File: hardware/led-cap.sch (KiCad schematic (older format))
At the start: 10 parts, among them IC1 ATTINY20-X, K1 CONN_3, P1 CONN_2, P2 CONN_6, Q1 IRLML2402PbF, U1 MMA7660

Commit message: Preliminary layout
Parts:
- removed P2: CONN_6, symbol CONN_6
- added K2: CONN_3, prgm:bcProgramHeader, symbol CONN_3
- added K3: CONN_3, prgm:bcProgramHeader_bottom, symbol CONN_3
- C1, C2: footprint (none) -> Capacitors_SMD:C_0805_HandSoldering
- IC1: footprint TSSOP14 -> tssop-14:TSSOP14
- K1: footprint (none) -> Connect:GS3
- P1: footprint (none) -> mods.pretty:AA Box
- Q1: footprint SOT-23 -> SMD_Packages:SOT-323
- R1, R2: footprint (none) -> Resistors_SMD:R_0603_HandSoldering
- U1: footprint (none) -> mods:DFN-10
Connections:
- net GND: now also K3.3 (P3)
- net VCC: now also K2.2 (PM)
- net LED_DATA: now reaches IC1.10 ((PCINT3/ADC3)PA3), K1.2 (PM)
- net Accel_INT: now reaches IC1.11 ((PCINT2/AIN1/ADC2)PA2), U1.5 (INT)
- net SCL: now reaches IC1.12 ((PCINT1/AIN0/ADC1)PA1), R2.2, U1.6 (SCL)
- net SDA: now reaches IC1.13 ((PCINT0/ADC0)PA0), R1.2, U1.7 (SDA)
- net MOSI: now reaches IC1.3 ((PCINT9/TPIDATA/MOSI/SDA/OC1A)PB1)
- net MOSI: now also K3.1 (P1)
- net RST: now reaches IC1.4 ((PCINT11/~RESET~)PB3)
- net RST: now also K3.2 (PM)
- net MISO: now reaches IC1.5 ((PCINT10/INT0/MISO/OC1B/OC0A/CKOUT)PB2)
- net MISO: now also K2.1 (P1)
- net SCLK: now reaches IC1.6 ((PCINT7/SCL/SCK/T1/ICP1/OC0B/ADC7)PA7)
- net SCLK: now also K2.3 (P3)
- net LED_CTRL: now reaches IC1.9 ((PCINT4/ADC4)PA4), Q1.1 (G)
- net LED_GND: now reaches K1.3 (P3), Q1.3 (D)
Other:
- note removed: "GND\n"
- note removed: "MISO\n"
- note removed: "MOSI"
- note removed: "RST\n"
- note removed: "SCK"
- note removed: "VCC"
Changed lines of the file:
@@
 LIBS:valves
 LIBS:mma7660
+LIBS:led-cap-cache
 EELAYER 24 0
 EELAYER END
@@
 F 0 "IC1" H 2900 4800 40  0000 C CNN
 F 1 "ATTINY20-X" H 4650 3300 40  0000 C CNN
-F 2 "TSSOP14" H 3850 4150 35  0000 C CIN
+F 2 "tssop-14:TSSOP14" H 3850 4150 35  0000 C CIN
 F 3 "" H 3850 4050 60  0000 C CNN
 	1    3850 4050
@@
 F 0 "C1" H 2550 3850 40  0000 L CNN
 F 1 ".1u" H 2556 3665 40  0000 L CNN
-F 2 "" H 2588 3600 30  0000 C CNN
+F 2 "Capacitors_SMD:C_0805_HandSoldering" H 2588 3600 30  0001 C CNN
 F 3 "" H 2550 3750 60  0000 C CNN
 	1    2550 3750
@@
 F 0 "C2" H 8450 4000 40  0000 L CNN
 F 1 "1u" H 8456 3815 40  0000 L CNN
-F 2 "" H 8488 3750 30  0000 C CNN
+F 2 "Capacitors_SMD:C_0805_HandSoldering" H 8488 3750 30  0001 C CNN
 F 3 "" H 8450 3900 60  0000 C CNN
 	1    8450 3900
@@
 F 0 "R1" V 5330 3050 40  0000 C CNN
 F 1 "2k2" V 5257 3051 40  0000 C CNN
-F 2 "" V 5180 3050 30  0000 C CNN
+F 2 "Resistors_SMD:R_0603_HandSoldering" V 5180 3050 30  0001 C CNN
 F 3 "" H 5250 3050 30  0000 C CNN
 	1    5250 3050
@@
 F 0 "R2" V 5580 3050 40  0000 C CNN
 F 1 "2k2" V 5507 3051 40  0000 C CNN
-F 2 "" V 5430 3050 30  0000 C CNN
+F 2 "Resistors_SMD:R_0603_HandSoldering" V 5430 3050 30  0001 C CNN
 F 3 "" H 5500 3050 30  0000 C CNN
 	1    5500 3050
@@
 F 0 "P1" V 3550 2900 40  0000 C CNN
 F 1 "CONN_2" V 3650 2900 40  0000 C CNN
-F 2 "" H 3600 2900 60  0000 C CNN
+F 2 "mods.pretty:AA Box" H 3600 2900 60  0001 C CNN
 F 3 "" H 3600 2900 60  0000 C CNN
 	1    3600 2900
@@
 F 0 "K1" V 8000 3850 50  0000 C CNN
 F 1 "CONN_3" V 8100 3850 40  0000 C CNN
-F 2 "" H 8050 3850 60  0000 C CNN
+F 2 "Connect:GS3" H 8050 3850 60  0001 C CNN
 F 3 "" H 8050 3850 60  0000 C CNN
 	1    8050 3850
-	1    0    0    -1
-$EndComp
-$Comp
-L CONN_6 P2
-U 1 1 54E77A45
-P 6250 4600
-F 0 "P2" V 6200 4600 60  0000 C CNN
-F 1 "CONN_6" V 6300 4600 60  0000 C CNN
-F 2 "" H 6250 4600 60  0000 C CNN
-F 3 "" H 6250 4600 60  0000 C CNN
-	1    6250 4600
 	1    0    0    -1
 $EndComp
@@
 F 0 "U1" H 6350 3000 60  0000 C CNN
 F 1 "MMA7660" H 6500 3650 60  0000 C CNN
-F 2 "" H 6750 3150 60  0000 C CNN
+F 2 "mods:DFN-10" H 6750 3150 60  0001 C CNN
 F 3 "" H 6750 3150 60  0000 C CNN
 	1    6700 3350
@@
 	2550 3450 2700 3450
 Wire Wire Line
-	2550 3300 2550 3450
-Wire Wire Line
-	2550 3450 2550 3550
+	2550 3300 2550 3550
 $Comp
 L GND #PWR2
@@
 	5550 4150 5000 4150
 Wire Wire Line
-	5900 4650 5450 4650
-Wire Wire Line
-	5450 4650 5450 4450
+	5900 4700 5450 4700
+Wire Wire Line
+	5450 4700 5450 4450
 Wire Wire Line
 	5450 4450 5000 4450
 Wire Wire Line
-	5900 4750 5200 4750
-Wire Wire Line
-	5200 4750 5200 4650
+	5900 4800 5200 4800
+Wire Wire Line
+	5200 4800 5200 4650
 Wire Wire Line
 	5200 4650 5000 4650
 Wire Wire Line
-	5900 4850 5800 4850
-Wire Wire Line
-	5800 4850 5800 4950
+	5900 4900 5750 4900
+Wire Wire Line
+	5750 4900 5750 5000
 $Comp
 L VCC #PWR8
@@
 $EndComp
 $Comp
-L GND #PWR10
+L GND #PWR9
 U 1 1 54E77FCD
-P 5800 4950
-F 0 "#PWR10" H 5800 4950 30  0001 C CNN
-F 1 "GND" H 5800 4880 30  0001 C CNN
-F 2 "" H 5800 4950 60  0000 C CNN
-F 3 "" H 5800 4950 60  0000 C CNN
-	1    5800 4950
-	1    0    0    -1
-$EndComp
-Text Notes 5750 4350 0    60   ~ 0
-MISO\n
-Text Notes 5750 4450 0    60   ~ 0
-VCC
-Text Notes 5750 4550 0    60   ~ 0
-SCK
-Text Notes 5750 4650 0    60   ~ 0
-MOSI
-Text Notes 5750 4750 0    60   ~ 0
-RST\n
-Text Notes 5750 4850 0    60   ~ 0
-GND\n
-Wire Wire Line
-	5000 3450 5250 3450
-Wire Wire Line
-	5250 3450 5950 3450
-Wire Wire Line
-	5000 3550 5500 3550
-Wire Wire Line
-	5500 3550 5950 3550
+P 5750 5000
+F 0 "#PWR9" H 5750 5000 30  0001 C CNN
+F 1 "GND" H 5750 4930 30  0001 C CNN
+F 2 "" H 5750 5000 60  0000 C CNN
+F 3 "" H 5750 5000 60  0000 C CNN
+	1    5750 5000
+	1    0    0    -1
+$EndComp
+Wire Wire Line
+	5000 3450 5950 3450
+Wire Wire Line
+	5000 3550 5950 3550
 Wire Wire Line
 	7400 3550 7400 3750
@@
 	7700 4600 7700 4500
 Wire Wire Line
-	7700 3500 7700 3600
-Wire Wire Line
-	7700 3600 7700 3750
+	7700 3500 7700 3750
 Wire Wire Line
 	5250 3300 5250 3450
@@
 $EndComp
 $Comp
-L VCC #PWR9
+L VCC #PWR10
 U 1 1 54E7825F
 P 5800 2800
-F 0 "#PWR9" H 5800 2900 30  0001 C CNN
+F 0 "#PWR10" H 5800 2900 30  0001 C CNN
 F 1 "VCC" H 5800 2900 30  0000 C CNN
 F 2 "" H 5800 2800 60  0000 C CNN
@@
 F 0 "Q1" H 7600 4151 40  0000 R CNN
 F 1 "IRLML2402PbF" H 8250 4350 40  0000 R CNN
-F 2 "SOT-23" H 7470 4402 29  0000 C CNN
+F 2 "SMD_Packages:SOT-323" H 7470 4402 29  0000 C CNN
 F 3 "" H 7600 4300 60  0000 C CNN
 	1    7600 4300
 	1    0    0    -1
 $EndComp
+$Comp
+L CONN_3 K2
+U 1 1 54EDFF11
+P 6250 4450
+F 0 "K2" V 6200 4450 50  0000 C CNN
+F 1 "CONN_3" V 6300 4450 40  0000 C CNN
+F 2 "prgm:bcProgramHeader" H 6250 4450 60  0001 C CNN
+F 3 "" H 6250 4450 60  0000 C CNN
+	1    6250 4450
+	1    0    0    -1
+$EndComp
+$Comp
+L CONN_3 K3
+U 1 1 54EDFFA4
+P 6250 4800
+F 0 "K3" V 6200 4800 50  0000 C CNN
+F 1 "CONN_3" V 6300 4800 40  0000 C CNN
+F 2 "prgm:bcProgramHeader_bottom" H 6250 4800 60  0001 C CNN
+F 3 "" H 6250 4800 60  0000 C CNN
+	1    6250 4800
+	1    0    0    -1
+$EndComp
+Text Label 5600 3450 0    60   ~ 0
+SDA
+Text Label 5600 3550 0    60   ~ 0
+SCL
+Text Label 5750 4350 0    60   ~ 0
+MISO
+Text Label 5750 4700 0    60   ~ 0
+MOSI
+Text Label 5750 4800 0    60   ~ 0
+RST
+Text Label 5750 4900 0    60   ~ 0
+GND
+Text Label 5750 4450 0    60   ~ 0
+VCC
+Text Label 5750 4550 0    60   ~ 0
+SCLK
+Text Label 5100 3750 0    60   ~ 0
+LED_DATA
+Text Label 5100 3850 0    60   ~ 0
+LED_CTRL
+Text Label 6450 3750 0    60   ~ 0
+Accel_INT
+Text Label 7700 4100 0    60   ~ 0
+LED_GND
 $EndSCHEMATC

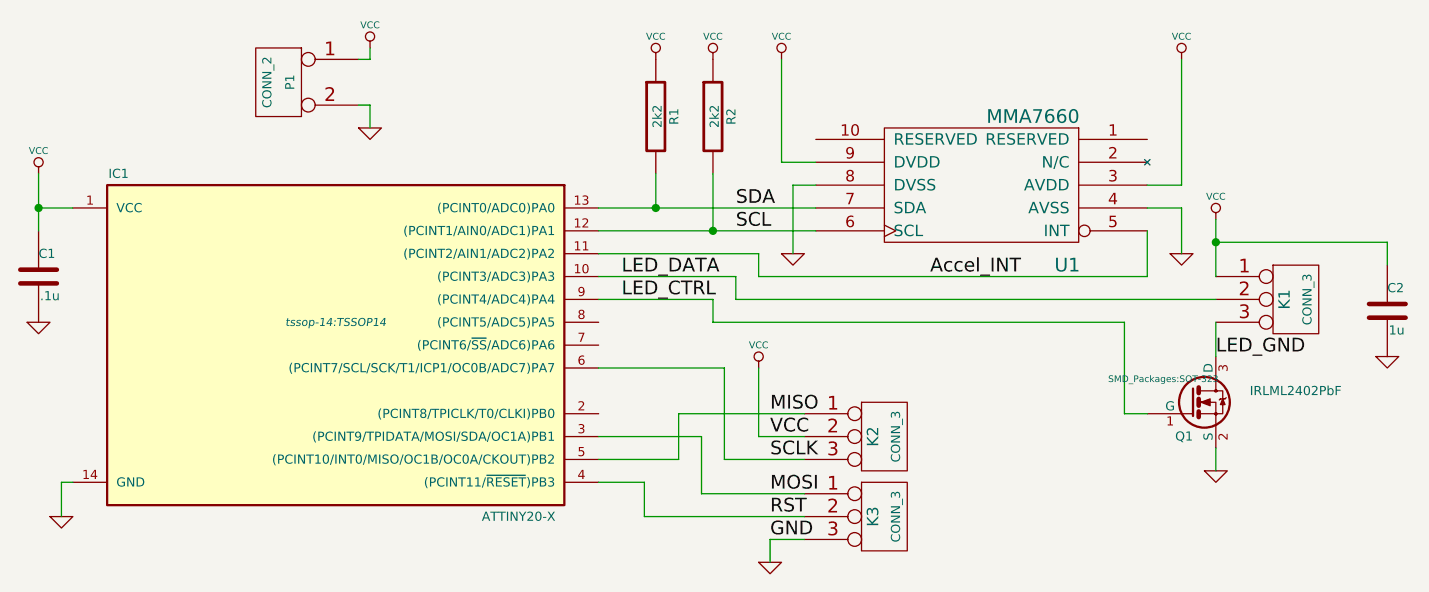
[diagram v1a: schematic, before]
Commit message: Updating based on Sheaff & Segee recommendations
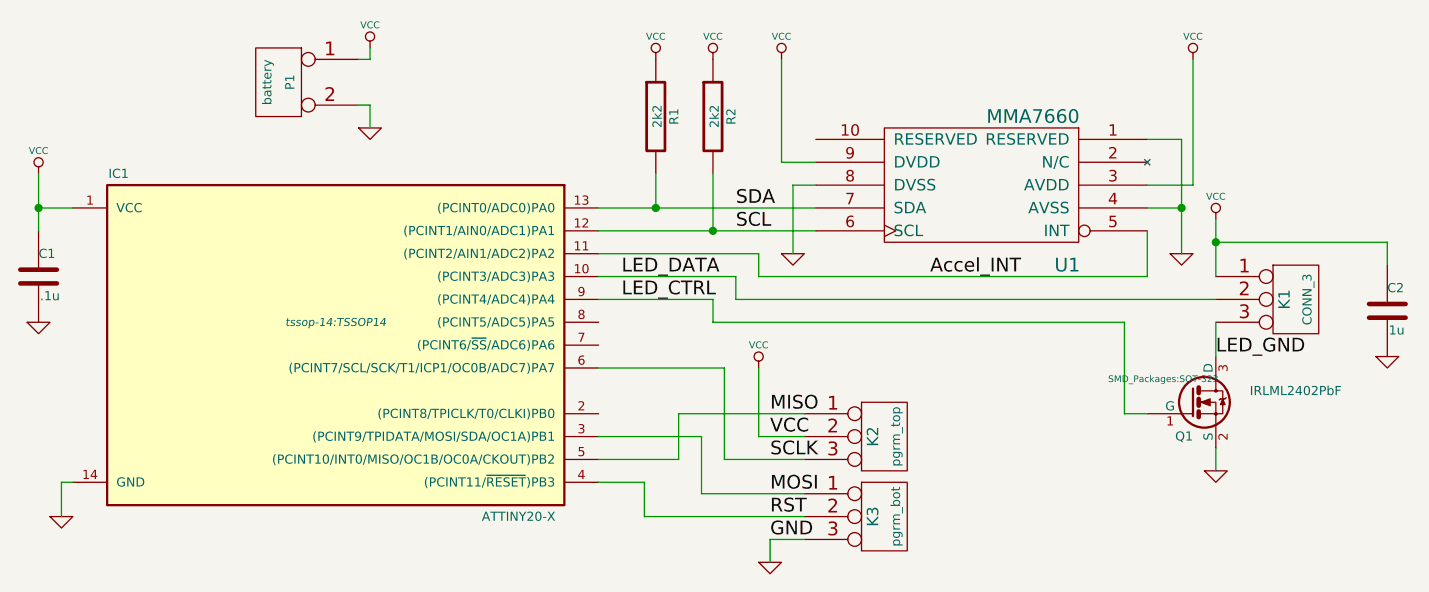
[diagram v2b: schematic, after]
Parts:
- K2: value CONN_3 -> pgrm_top
- K3: value CONN_3 -> pgrm_bot
- P1: value CONN_2 -> battery
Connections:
- net GND: now also U1.1 (RESERVED)
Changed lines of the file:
@@
 P 3600 2900
 F 0 "P1" V 3550 2900 40  0000 C CNN
-F 1 "CONN_2" V 3650 2900 40  0000 C CNN
+F 1 "battery" V 3650 2900 40  0000 C CNN
 F 2 "mods.pretty:AA Box" H 3600 2900 60  0001 C CNN
 F 3 "" H 3600 2900 60  0000 C CNN
@@
 $EndComp
 $Comp
-L GND #PWR3
+L GND #PWR01
 U 1 1 54E77E6C
 P 2650 4800
-F 0 "#PWR3" H 2650 4800 30  0001 C CNN
+F 0 "#PWR01" H 2650 4800 30  0001 C CNN
 F 1 "GND" H 2650 4730 30  0001 C CNN
 F 2 "" H 2650 4800 60  0000 C CNN
@@
 	1    0    0    -1
 $EndComp
-Wire Wire Line
-	2700 4650 2650 4650
-Wire Wire Line
-	2650 4650 2650 4800
-$Comp
-L VCC #PWR1
+$Comp
+L VCC #PWR02
 U 1 1 54E77E87
 P 2550 3300
-F 0 "#PWR1" H 2550 3400 30  0001 C CNN
+F 0 "#PWR02" H 2550 3400 30  0001 C CNN
 F 1 "VCC" H 2550 3400 30  0000 C CNN
 F 2 "" H 2550 3300 60  0000 C CNN
@@
 	1    0    0    -1
 $EndComp
-Wire Wire Line
-	2550 3450 2700 3450
-Wire Wire Line
-	2550 3300 2550 3550
-$Comp
-L GND #PWR2
+$Comp
+L GND #PWR03
 U 1 1 54E77E9E
 P 2550 3950
-F 0 "#PWR2" H 2550 3950 30  0001 C CNN
+F 0 "#PWR03" H 2550 3950 30  0001 C CNN
 F 1 "GND" H 2550 3880 30  0001 C CNN
 F 2 "" H 2550 3950 60  0000 C CNN
@@
 $EndComp
 $Comp
-L GND #PWR5
+L GND #PWR04
 U 1 1 54E77EB1
 P 4000 3100
-F 0 "#PWR5" H 4000 3100 30  0001 C CNN
+F 0 "#PWR04" H 4000 3100 30  0001 C CNN
 F 1 "GND" H 4000 3030 30  0001 C CNN
 F 2 "" H 4000 3100 60  0000 C CNN
@@
 $EndComp
 $Comp
-L VCC #PWR4
+L VCC #PWR05
 U 1 1 54E77EBE
 P 4000 2750
-F 0 "#PWR4" H 4000 2850 30  0001 C CNN
+F 0 "#PWR05" H 4000 2850 30  0001 C CNN
 F 1 "VCC" H 4000 2850 30  0000 C CNN
 F 2 "" H 4000 2750 60  0000 C CNN
@@
 	1    0    0    -1
 $EndComp
-Wire Wire Line
-	3950 2800 4000 2800
-Wire Wire Line
-	4000 2800 4000 2750
-Wire Wire Line
-	3950 3000 4000 3000
-Wire Wire Line
-	4000 3000 4000 3100
-Wire Wire Line
-	5000 4550 5350 4550
-Wire Wire Line
-	5350 4550 5350 4350
-Wire Wire Line
-	5350 4350 5900 4350
-Wire Wire Line
-	5900 4450 5700 4450
-Wire Wire Line
-	5700 4450 5700 4150
-Wire Wire Line
-	5900 4550 5550 4550
-Wire Wire Line
-	5550 4550 5550 4150
-Wire Wire Line
-	5550 4150 5000 4150
-Wire Wire Line
-	5900 4700 5450 4700
-Wire Wire Line
-	5450 4700 5450 4450
-Wire Wire Line
-	5450 4450 5000 4450
-Wire Wire Line
-	5900 4800 5200 4800
-Wire Wire Line
-	5200 4800 5200 4650
-Wire Wire Line
-	5200 4650 5000 4650
-Wire Wire Line
-	5900 4900 5750 4900
-Wire Wire Line
-	5750 4900 5750 5000
-$Comp
-L VCC #PWR8
+$Comp
+L VCC #PWR06
 U 1 1 54E77FB7
 P 5700 4150
-F 0 "#PWR8" H 5700 4250 30  0001 C CNN
+F 0 "#PWR06" H 5700 4250 30  0001 C CNN
 F 1 "VCC" H 5700 4250 30  0000 C CNN
 F 2 "" H 5700 4150 60  0000 C CNN
@@
 $EndComp
 $Comp
-L GND #PWR9
+L GND #PWR07
 U 1 1 54E77FCD
 P 5750 5000
-F 0 "#PWR9" H 5750 5000 30  0001 C CNN
+F 0 "#PWR07" H 5750 5000 30  0001 C CNN
 F 1 "GND" H 5750 4930 30  0001 C CNN
 F 2 "" H 5750 5000 60  0000 C CNN
@@
 	1    0    0    -1
 $EndComp
-Wire Wire Line
-	5000 3450 5950 3450
-Wire Wire Line
-	5000 3550 5950 3550
-Wire Wire Line
-	7400 3550 7400 3750
-Wire Wire Line
-	7400 3750 5700 3750
-Wire Wire Line
-	5700 3750 5700 3650
-Wire Wire Line
-	5700 3650 5000 3650
-Wire Wire Line
-	5000 3750 5600 3750
-Wire Wire Line
-	5600 3750 5600 3850
-Wire Wire Line
-	5600 3850 7700 3850
-Wire Wire Line
-	7700 3950 7700 4100
-Wire Wire Line
-	5000 3850 5500 3850
-Wire Wire Line
-	5500 3850 5500 3950
-Wire Wire Line
-	5500 3950 7300 3950
-Wire Wire Line
-	7300 3950 7300 4350
-Wire Wire Line
-	7300 4350 7400 4350
-$Comp
-L VCC #PWR14
+$Comp
+L VCC #PWR08
 U 1 1 54E78138
 P 7700 3500
-F 0 "#PWR14" H 7700 3600 30  0001 C CNN
+F 0 "#PWR08" H 7700 3600 30  0001 C CNN
 F 1 "VCC" H 7700 3600 30  0000 C CNN
 F 2 "" H 7700 3500 60  0000 C CNN
@@
 $EndComp
 $Comp
-L GND #PWR15
+L GND #PWR09
 U 1 1 54E78143
 P 7700 4600
-F 0 "#PWR15" H 7700 4600 30  0001 C CNN
+F 0 "#PWR09" H 7700 4600 30  0001 C CNN
 F 1 "GND" H 7700 4530 30  0001 C CNN
 F 2 "" H 7700 4600 60  0000 C CNN
@@
 	1    0    0    -1
 $EndComp
-Wire Wire Line
-	7700 4600 7700 4500
-Wire Wire Line
-	7700 3500 7700 3750
-Wire Wire Line
-	5250 3300 5250 3450
-Connection ~ 5250 3450
-Wire Wire Line
-	5500 3300 5500 3550
-Connection ~ 5500 3550
-$Comp
-L VCC #PWR6
+$Comp
+L VCC #PWR010
 U 1 1 54E78219
 P 5250 2800
-F 0 "#PWR6" H 5250 2900 30  0001 C CNN
+F 0 "#PWR010" H 5250 2900 30  0001 C CNN
 F 1 "VCC" H 5250 2900 30  0000 C CNN
 F 2 "" H 5250 2800 60  0000 C CNN
@@
 $EndComp
 $Comp
-L VCC #PWR7
+L VCC #PWR011
 U 1 1 54E78224
 P 5500 2800
-F 0 "#PWR7" H 5500 2900 30  0001 C CNN
+F 0 "#PWR011" H 5500 2900 30  0001 C CNN
 F 1 "VCC" H 5500 2900 30  0000 C CNN
 F 2 "" H 5500 2800 60  0000 C CNN
@@
 $EndComp
 $Comp
-L VCC #PWR10
+L VCC #PWR012
 U 1 1 54E7825F
 P 5800 2800
-F 0 "#PWR10" H 5800 2900 30  0001 C CNN
+F 0 "#PWR012" H 5800 2900 30  0001 C CNN
 F 1 "VCC" H 5800 2900 30  0000 C CNN
 F 2 "" H 5800 2800 60  0000 C CNN
@@
 $EndComp
 $Comp
-L VCC #PWR12
+L VCC #PWR013
 U 1 1 54E7826A
-P 7550 2800
-F 0 "#PWR12" H 7550 2900 30  0001 C CNN
-F 1 "VCC" H 7550 2900 30  0000 C CNN
-F 2 "" H 7550 2800 60  0000 C CNN
-F 3 "" H 7550 2800 60  0000 C CNN
-	1    7550 2800
-	1    0    0    -1
-$EndComp
-Wire Wire Line
-	7400 3350 7550 3350
-Wire Wire Line
-	5950 3250 5800 3250
-Wire Wire Line
-	5800 3250 5800 2800
-$Comp
-L GND #PWR13
+P 7600 2800
+F 0 "#PWR013" H 7600 2900 30  0001 C CNN
+F 1 "VCC" H 7600 2900 30  0000 C CNN
+F 2 "" H 7600 2800 60  0000 C CNN
+F 3 "" H 7600 2800 60  0000 C CNN
+	1    7600 2800
+	1    0    0    -1
+$EndComp
+$Comp
+L GND #PWR014
 U 1 1 54E7830A
 P 7550 3650
-F 0 "#PWR13" H 7550 3650 30  0001 C CNN
+F 0 "#PWR014" H 7550 3650 30  0001 C CNN
 F 1 "GND" H 7550 3580 30  0001 C CNN
 F 2 "" H 7550 3650 60  0000 C CNN
@@
 $EndComp
 $Comp
-L GND #PWR11
+L GND #PWR015
 U 1 1 54E78315
 P 5850 3650
-F 0 "#PWR11" H 5850 3650 30  0001 C CNN
+F 0 "#PWR015" H 5850 3650 30  0001 C CNN
 F 1 "GND" H 5850 3580 30  0001 C CNN
 F 2 "" H 5850 3650 60  0000 C CNN
@@
 	1    0    0    -1
 $EndComp
-Wire Wire Line
-	5950 3350 5850 3350
-Wire Wire Line
-	5850 3350 5850 3650
-Wire Wire Line
-	7400 3450 7550 3450
-Wire Wire Line
-	7550 3450 7550 3650
-$Comp
-L GND #PWR16
+$Comp
+L GND #PWR016
 U 1 1 54E78405
 P 8450 4100
-F 0 "#PWR16" H 8450 4100 30  0001 C CNN
+F 0 "#PWR016" H 8450 4100 30  0001 C CNN
 F 1 "GND" H 8450 4030 30  0001 C CNN
 F 2 "" H 8450 4100 60  0000 C CNN
@@
 	1    0    0    -1
 $EndComp
-Wire Wire Line
-	7700 3600 8450 3600
-Wire Wire Line
-	8450 3600 8450 3700
-Connection ~ 7700 3600
-Wire Wire Line
-	7550 3350 7550 2800
-Connection ~ 2550 3450
 $Comp
 L BSS138 Q1
@@
 P 6250 4450
 F 0 "K2" V 6200 4450 50  0000 C CNN
-F 1 "CONN_3" V 6300 4450 40  0000 C CNN
+F 1 "pgrm_top" V 6300 4450 40  0000 C CNN
 F 2 "prgm:bcProgramHeader" H 6250 4450 60  0001 C CNN
 F 3 "" H 6250 4450 60  0000 C CNN
@@
 P 6250 4800
 F 0 "K3" V 6200 4800 50  0000 C CNN
-F 1 "CONN_3" V 6300 4800 40  0000 C CNN
+F 1 "pgrm_bot" V 6300 4800 40  0000 C CNN
 F 2 "prgm:bcProgramHeader_bottom" H 6250 4800 60  0001 C CNN
 F 3 "" H 6250 4800 60  0000 C CNN
@@
 Text Label 7700 4100 0    60   ~ 0
 LED_GND
+Wire Wire Line
+	2700 4650 2650 4650
+Wire Wire Line
+	2650 4650 2650 4800
+Wire Wire Line
+	2550 3450 2700 3450
+Wire Wire Line
+	2550 3300 2550 3550
+Wire Wire Line
+	3950 2800 4000 2800
+Wire Wire Line
+	4000 2800 4000 2750
+Wire Wire Line
+	3950 3000 4000 3000
+Wire Wire Line
+	4000 3000 4000 3100
+Wire Wire Line
+	5000 4550 5350 4550
+Wire Wire Line
+	5350 4550 5350 4350
+Wire Wire Line
+	5350 4350 5900 4350
+Wire Wire Line
+	5900 4450 5700 4450
+Wire Wire Line
+	5700 4450 5700 4150
+Wire Wire Line
+	5900 4550 5550 4550
+Wire Wire Line
+	5550 4550 5550 4150
+Wire Wire Line
+	5550 4150 5000 4150
+Wire Wire Line
+	5900 4700 5450 4700
+Wire Wire Line
+	5450 4700 5450 4450
+Wire Wire Line
+	5450 4450 5000 4450
+Wire Wire Line
+	5900 4800 5200 4800
+Wire Wire Line
+	5200 4800 5200 4650
+Wire Wire Line
+	5200 4650 5000 4650
+Wire Wire Line
+	5900 4900 5750 4900
+Wire Wire Line
+	5750 4900 5750 5000
+Wire Wire Line
+	5000 3450 5950 3450
+Wire Wire Line
+	5000 3550 5950 3550
+Wire Wire Line
+	7400 3550 7400 3750
+Wire Wire Line
+	7400 3750 5700 3750
+Wire Wire Line
+	5700 3750 5700 3650
+Wire Wire Line
+	5700 3650 5000 3650
+Wire Wire Line
+	5000 3750 5600 3750
+Wire Wire Line
+	5600 3750 5600 3850
+Wire Wire Line
+	5600 3850 7700 3850
+Wire Wire Line
+	7700 3950 7700 4100
+Wire Wire Line
+	5000 3850 5500 3850
+Wire Wire Line
+	5500 3850 5500 3950
+Wire Wire Line
+	5500 3950 7300 3950
+Wire Wire Line
+	7300 3950 7300 4350
+Wire Wire Line
+	7300 4350 7400 4350
+Wire Wire Line
+	7700 4600 7700 4500
+Wire Wire Line
+	7700 3500 7700 3750
+Wire Wire Line
+	5250 3300 5250 3450
+Connection ~ 5250 3450
+Wire Wire Line
+	5500 3300 5500 3550
+Connection ~ 5500 3550
+Wire Wire Line
+	7400 3350 7600 3350
+Wire Wire Line
+	5950 3250 5800 3250
+Wire Wire Line
+	5800 3250 5800 2800
+Wire Wire Line
+	5950 3350 5850 3350
+Wire Wire Line
+	5850 3350 5850 3650
+Wire Wire Line
+	7400 3450 7550 3450
+Wire Wire Line
+	7550 3150 7550 3650
+Wire Wire Line
+	7700 3600 8450 3600
+Wire Wire Line
+	8450 3600 8450 3700
+Connection ~ 7700 3600
+Wire Wire Line
+	7600 3350 7600 2800
+Connection ~ 2550 3450
+Wire Wire Line
+	7400 3150 7550 3150
+Connection ~ 7550 3450
 $EndSCHEMATC
